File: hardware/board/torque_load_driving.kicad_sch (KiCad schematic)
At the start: 10 parts

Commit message: update board schematic
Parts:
- removed R?: 0R, symbol Device:R
- added C1: 300pF, Capacitor_SMD:C_0402_1005Metric, symbol Device:C
- added R5, R6: 100, Resistor_SMD:R_0402_1005Metric, symbol Device:R
- added R7, R8, R9: 49.9, Resistor_SMD:R_0402_1005Metric, symbol Device:R
- added TP1: TestPoint, kicad_component_library:TestPoint_Keystone_5027_Miniature, symbol Connector:TestPoint
- added U1: ADS7049, Package_SO:VSSOP-8_2.3x2mm_P0.5mm, symbol Analog_ADC:ADS7049
- U?: Manufacturer (none) -> Texas Instruments; Manufacturer Number (none) -> INA180A1IDBVT; manufacturer Texas Instruments -> (none); manufacturer number INA180A1IDBVT -> (none)
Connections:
- net GNDPWR is gone; now on net GND: Q?.1 (S), Q?.2 (S), Q?.3 (S), U?.2 (GND)
- net +3V3: now also U1.1 (DVDD)
- net at U?.1: now also R5.2, TP1.1
- net GNDD renamed GND
- net GND: now also R6.1, U1.8 (GND)
- new net: C1.1, R5.1, U1.6 (AINP)
- new net: R9.1, U1.4 (~{CS})
- new net: C1.2, R6.2, U1.5 (AINM)
- new net: R8.1, U1.2 (SCLK)
- new net: R7.1, U1.3 (SDO)
- new net ADC_CS: R9.2
- new net ADC_POCI: R7.2
- new net ADC_SCK: R8.2
- new net VREF_3V3: U1.7 (AVDD)
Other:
- note added: "Note: test point output will look slightly distorted with small transient spikes when the ADS7049 is acquiring samples."
- note added: "U13 must be driven by a low impedance source and requires ~300pF input capacitance for stability."
- moved on the sheet: J?

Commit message: update pcb
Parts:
- removed D?: DIODE, symbol pspice:DIODE
- added C?: 0.1uF, symbol Device:C
- added D5: D, symbol Device:D
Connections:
- net +3V3: now also C?.1
- net GND: now also C?.2
- net at D?.2 (A), J?.1 (Pin_1), R?.2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: now also D5.1 (K)
- net at J?.2 (Pin_2), Q?.5 (D), Q?.6 (D)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: now also D5.2 (A)
- net VPP renamed +12V
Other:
- note added: "Current Sense Bypass Cap"
- note added: "FIXME: do we need this Zener?"
- note added: "Gain: 20"

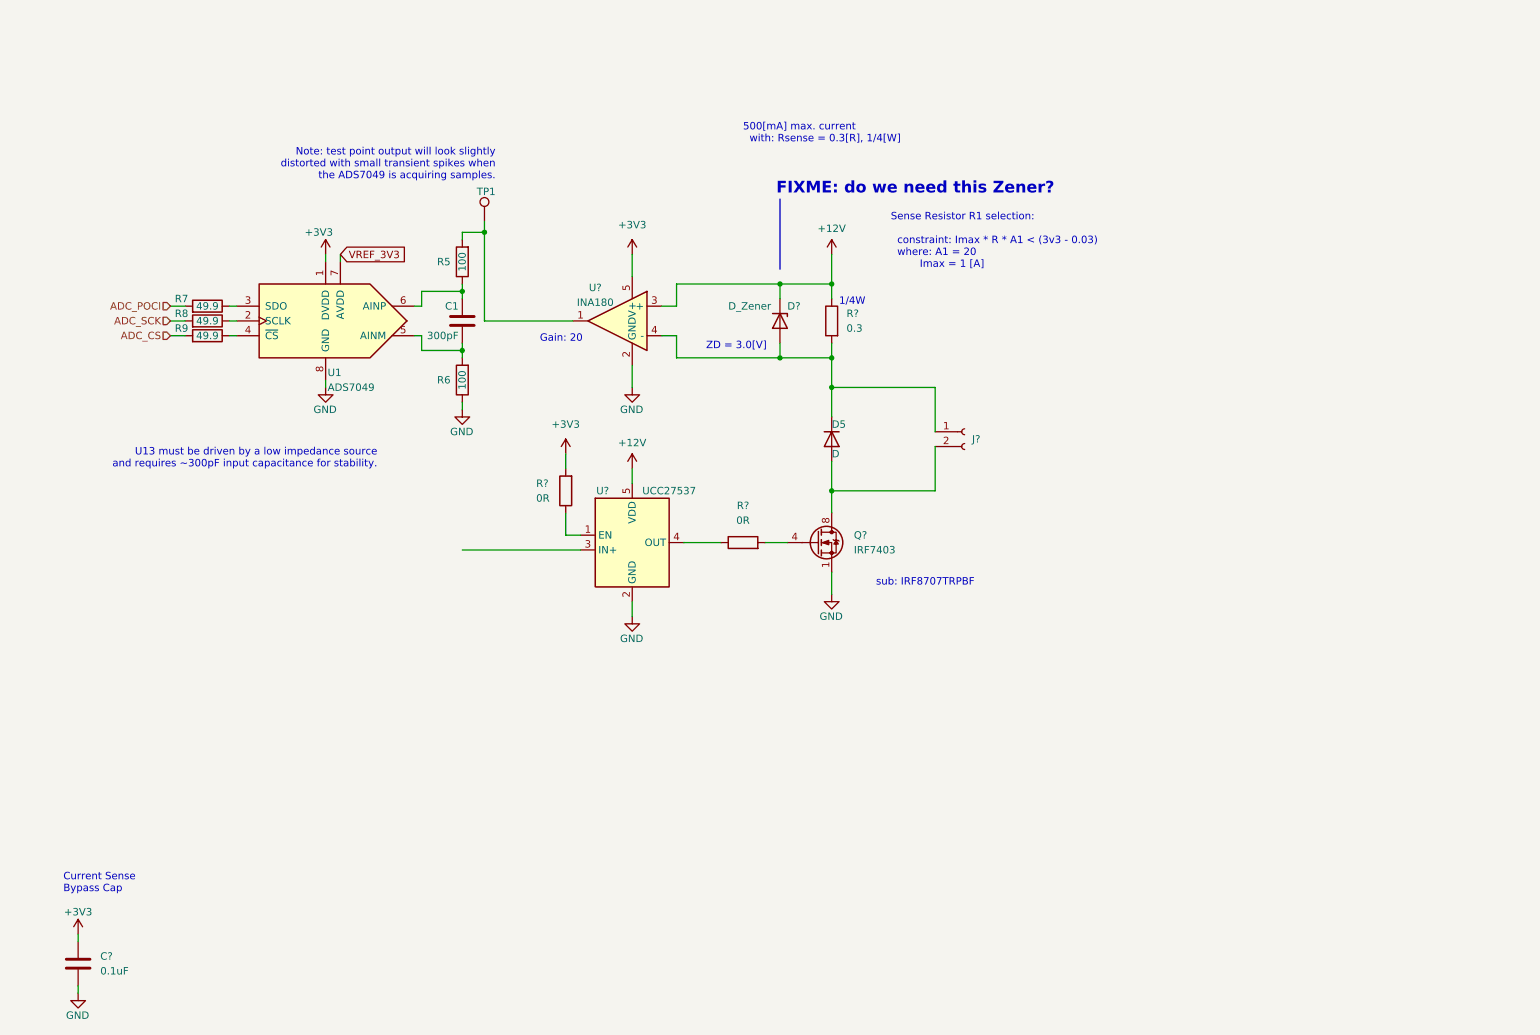
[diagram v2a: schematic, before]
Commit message: update schematic
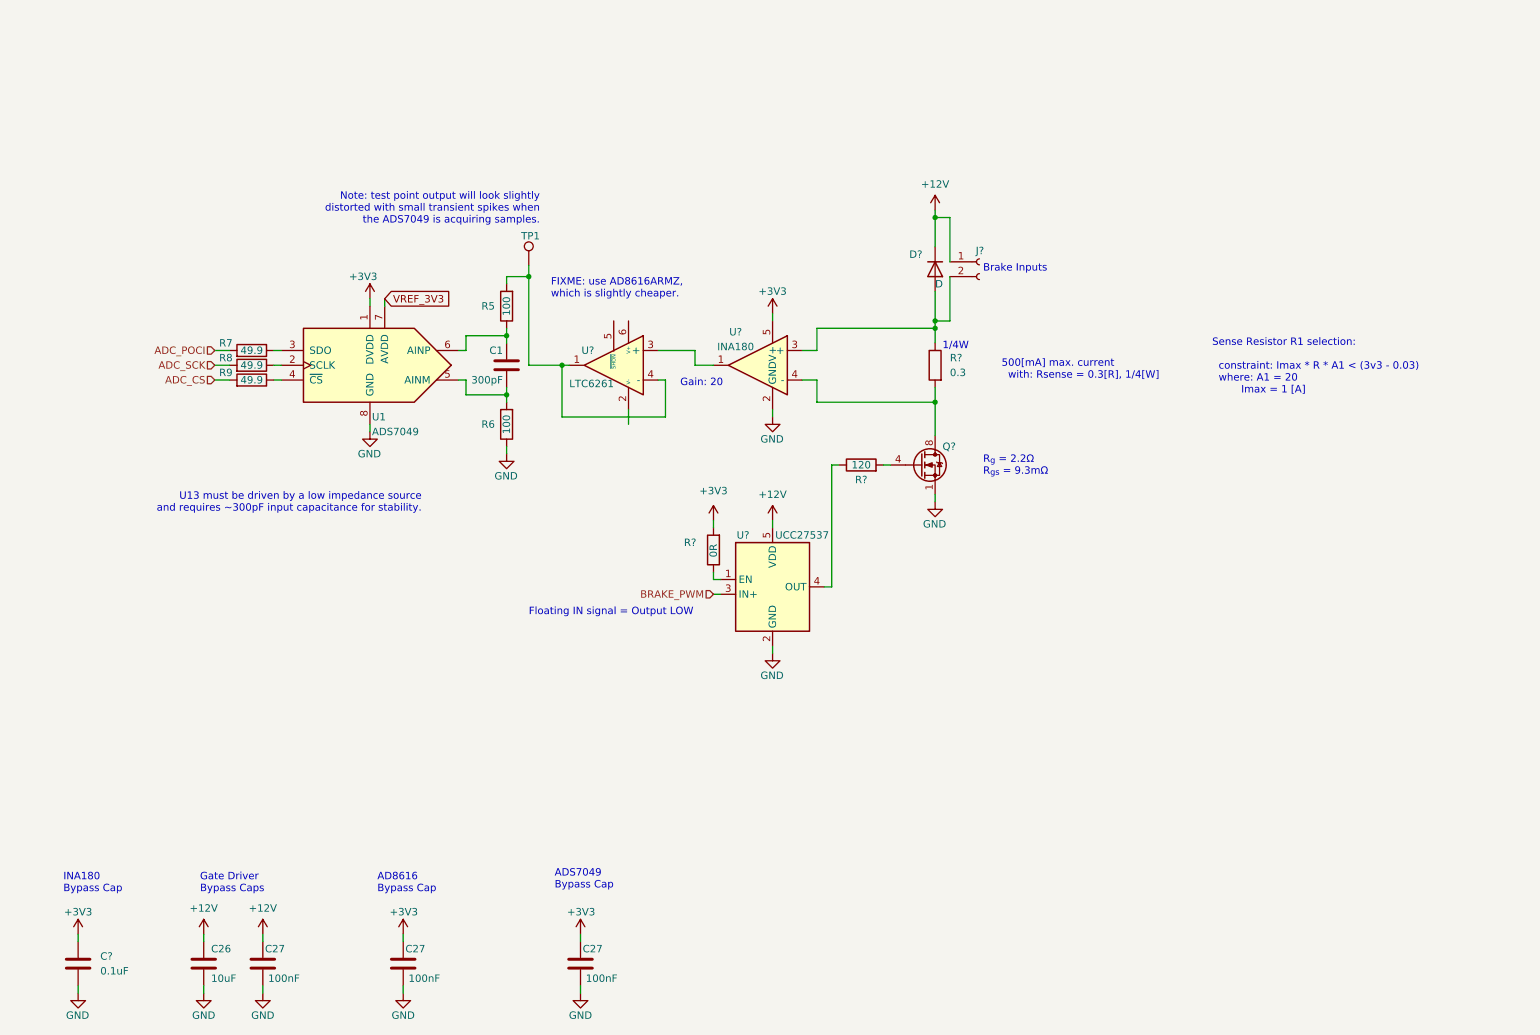
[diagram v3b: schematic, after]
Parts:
- removed D?: D_Zener, symbol Device:D_Zener
- added C26: 10uF, Capacitor_SMD:C_0805_2012Metric, symbol Device:C
- added C27 (x3): 100nF, Capacitor_SMD:C_0402_1005Metric, symbol Device:C
- added U?: LTC6261, Package_TO_SOT_SMD:TSOT-23-6_HandSoldering, symbol kicad_component_library:LTC6261
- Q?: value IRF7403 -> IRF8707TRPBF; link https://www.digikey.com/en/products/detail/infineon-technologies/IRF7403TRPBF/812739 -> https://www.digikey.com/en/products/detail/infineon-technologies/IRF8707TRPBF/1925376
- R?: value 0R -> 120; footprint (none) -> Resistor_SMD:R_2512_6332Metric; Link (none) -> https://www.digikey.com/en/products/detail/te-connectivity-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; Manufacturer (none) -> TE Connectivity Passive Product; Manufacturer Number (none) -> 3521120RFT
- U?: Link (none) -> https://www.digikey.com/en/products/detail/texas-instrument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; Manufacturer (none) -> Texas Instruments; Manufacturer Number (none) -> UCC27537DBVR
- renumbered D5 to D?
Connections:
- net +12V: now also D?.1 (K), J?.1 (Pin_1), C26.1, C27.2; no longer R?.1, U?.3 (+)
- net +3V3: now also C27.2, C27.2
- net GND: now also C26.2, C27.1, C27.1, C27.1
- net at R?.2, U?.4 (-): now also Q?.5 (D), Q?.6 (D), Q?.7 (D), Q?.8 (D); no longer D?.1 (K), J?.1 (Pin_1)
- net at R5.2, TP1.1: now also U?.1, U?.4 (-); no longer U?.1
- net BRAKE_PWM: now reaches U?.3 (IN+)
- new net: D?.2 (A), J?.2 (Pin_2), R?.1, U?.3 (+)
- new net: U?.1, U?.3 (+)
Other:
- note added: "AD8616 Bypass Cap"
- note added: "ADS7049 Bypass Cap"
- note added: "Brake Inputs"
- note added: "FIXME: use AD8616ARMZ, which is slightly cheaper."
- note added: "Floating IN signal = Output LOW"
- note added: "Gate Driver Bypass Caps"
- note added: "INA180 Bypass Cap"
- note added: "R_{g} = 2.2Ω R_{gs} = 9.3mΩ"
- note removed: "Current Sense Bypass Cap"
- note removed: "FIXME: do we need this Zener?"
- note removed: "ZD = 3.0[V]"
- note removed: "sub: IRF8707TRPBF"
- moved on the sheet: C1, D?, J?, Q?, R5, R6, R7, R8, R9, R?, TP1, U1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

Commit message: update schematic
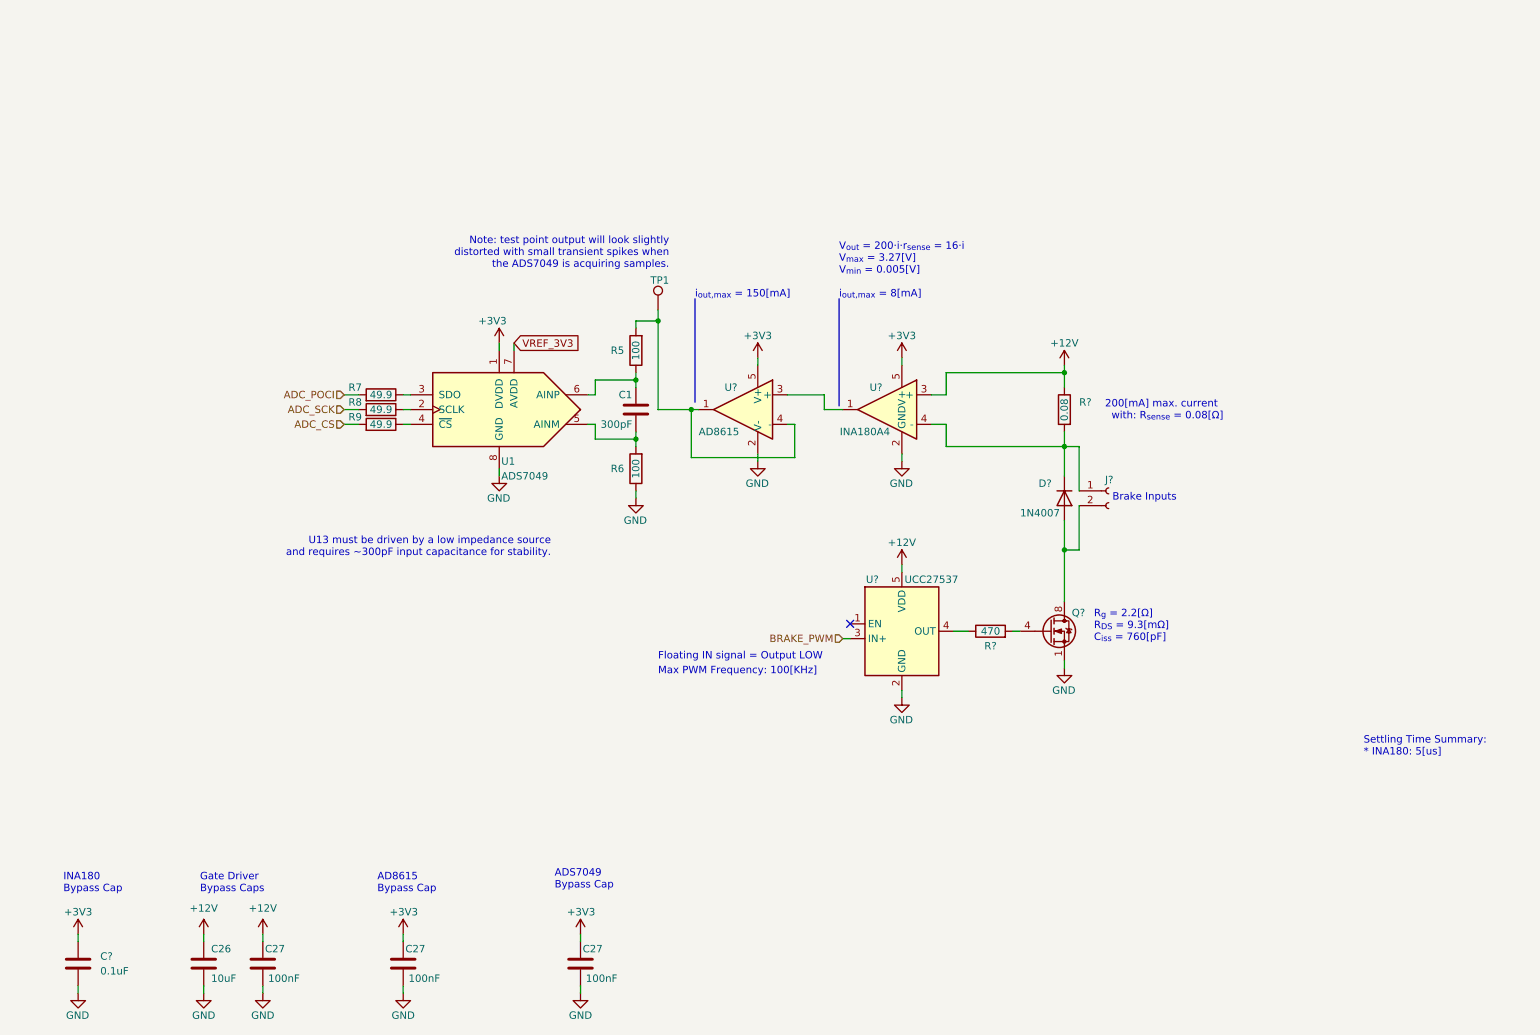
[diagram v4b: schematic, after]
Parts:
- removed R?: 0R, symbol Device:R
- removed U?: LTC6261, Package_TO_SOT_SMD:TSOT-23-6_HandSoldering, symbol kicad_component_library:LTC6261
- added U?: AD8615, Package_TO_SOT_SMD:TSOT-23-5, symbol kicad_component_library:AD8615
- D?: value D -> 1N4007; footprint (none) -> Diode_SMD:D_SOD-123F; Link (none) -> https://www.digikey.com/en/products/detail/smc-diode-soluti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; Manufacturer (none) -> SMC Diode Solutions; Manufacturer Number (none) -> 1N4007FL
- R?: value 0.3 -> 0.08; footprint (none) -> Resistor_SMD:R_1206_3216Metric; Link (none) -> https://www.digikey.com/en/products/detail/vishay-dale/WSL1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; Manufacturer (none) -> Vishay Dale; Manufacturer Number (none) -> WSL1206R0800FEA18; Power Dissipation (none) -> 1/2W; link https://www.digikey.com/en/products/detail/panasonic-electr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 -> (none); manufacturer Panasonic Electronic Components -> (none); manufacturer number ERJ-3BQFR30V -> (none)
- R?: value 120 -> 470; footprint Resistor_SMD:R_2512_6332Metric -> Resistor_SMD:R_0805_2012Metric; Link https://www.digikey.com/en/products/detail/te-connectivity-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 -> https://www.digikey.com/en/products/detail/koa-speer-electr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; Manufacturer TE Connectivity Passive Product -> Panasonic Electronic Components; Manufacturer Number 3521120RFT -> SG73P2ATTD4700F; Power (none) -> 1/2W; Tolerance (none) -> 1%
- U?: value INA180 -> INA180A4; Manufacturer Number INA180A1IDBVT -> INA180A4IDBVT; Notes (none) -> Fixed Gain: 200V/V; link https://www.digikey.com/en/products/detail/INA180A1IDBVT/29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 -> https://www.digikey.com/en/products/detail/texas-instrument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
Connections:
- net +12V: now also R?.1, U?.3 (+); no longer D?.1 (K), J?.1 (Pin_1)
- net +3V3: now also U?.5 (V+)
- net GND: now also U?.2 (V-)
- net at D?.2 (A), J?.2 (Pin_2): now also Q?.5 (D), Q?.6 (D), Q?.7 (D), Q?.8 (D); no longer R?.1, U?.3 (+)
- net at R5.2, TP1.1: now also U?.1, U?.4 (-)
- net at U?.1: now also U?.3 (+)
- new net: D?.1 (K), J?.1 (Pin_1), R?.2, U?.4 (-)
- no-connect marks 0 -> 1
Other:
- note added: "200[mA] max. current with: R_{sense} = 0.08[Ω]"
- note added: "AD8615 Bypass Cap"
- note added: "Max PWM Frequency: 100[KHz]"
- note added: "R_{g} = 2.2[Ω] R_{DS} = 9.3[mΩ] C_{iss} = 760[pF]"
- note added: "Settling Time Summary: * INA180: 5[us]"
- note added: "V_{out} = 200·i·r_{sense} = 16·i V_{max} = 3.27[V] V_{min} = 0.005[V] i_{out,max} = 8[mA]"
- note added: "i_{out,max} = 150[mA]"
- note removed: "1/4W"
- note removed: "500[mA] max. current with: Rsense = 0.3[R], 1/4[W]"
- note removed: "AD8616 Bypass Cap"
- note removed: "FIXME: use AD8616ARMZ, which is slightly cheaper."
- note removed: "Gain: 20"
- note removed: "R_{g} = 2.2Ω R_{gs} = 9.3mΩ"
- note removed: "Sense Resistor R1 selection: constraint: Imax * R * A1 < (3v3 - 0.03) where: A1 = 20 Imax = 1 [A]"
- moved on the sheet: C1, D?, J?, Q?, R5, R6, R7, R8, R9, R?, TP1, U1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
